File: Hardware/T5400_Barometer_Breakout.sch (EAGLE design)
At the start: 13 parts, among them U1 T5400

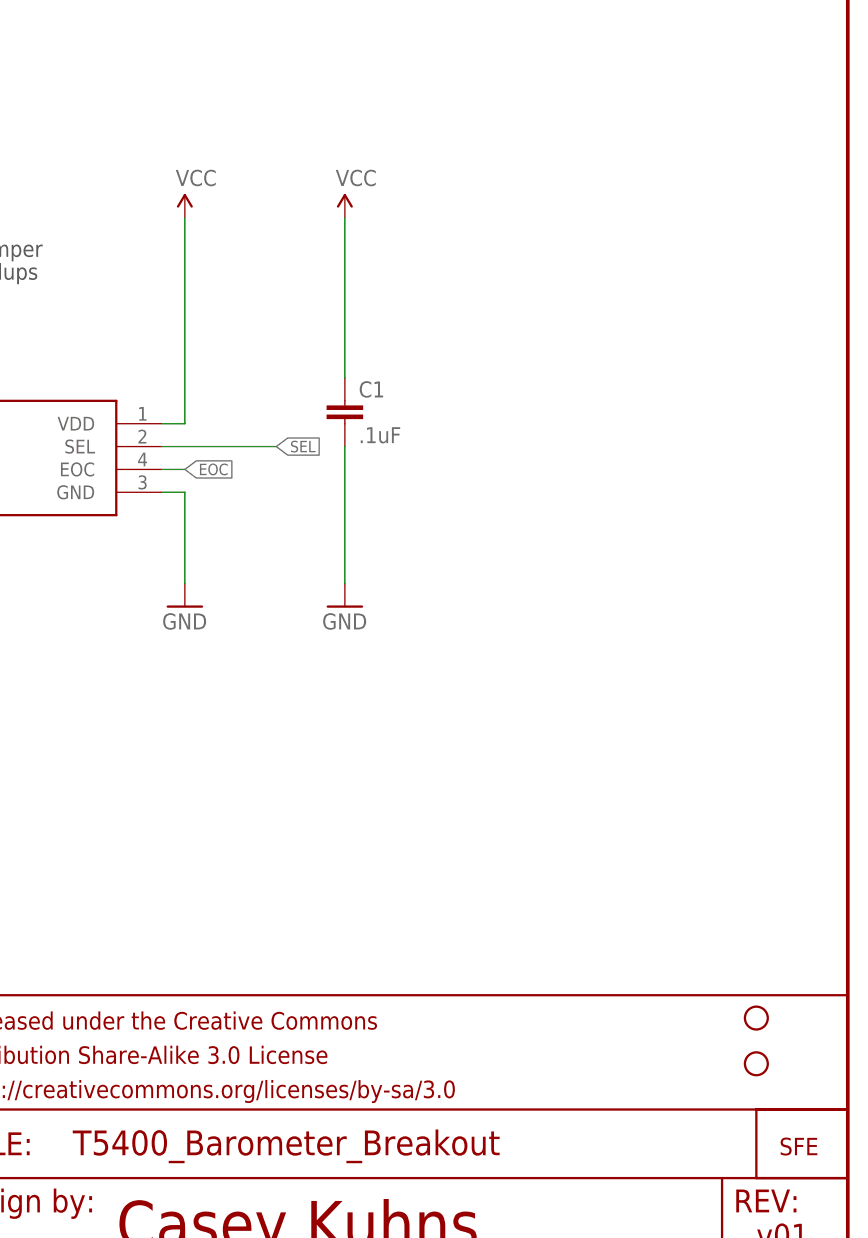
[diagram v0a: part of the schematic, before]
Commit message: updated with mode pullup and larger board
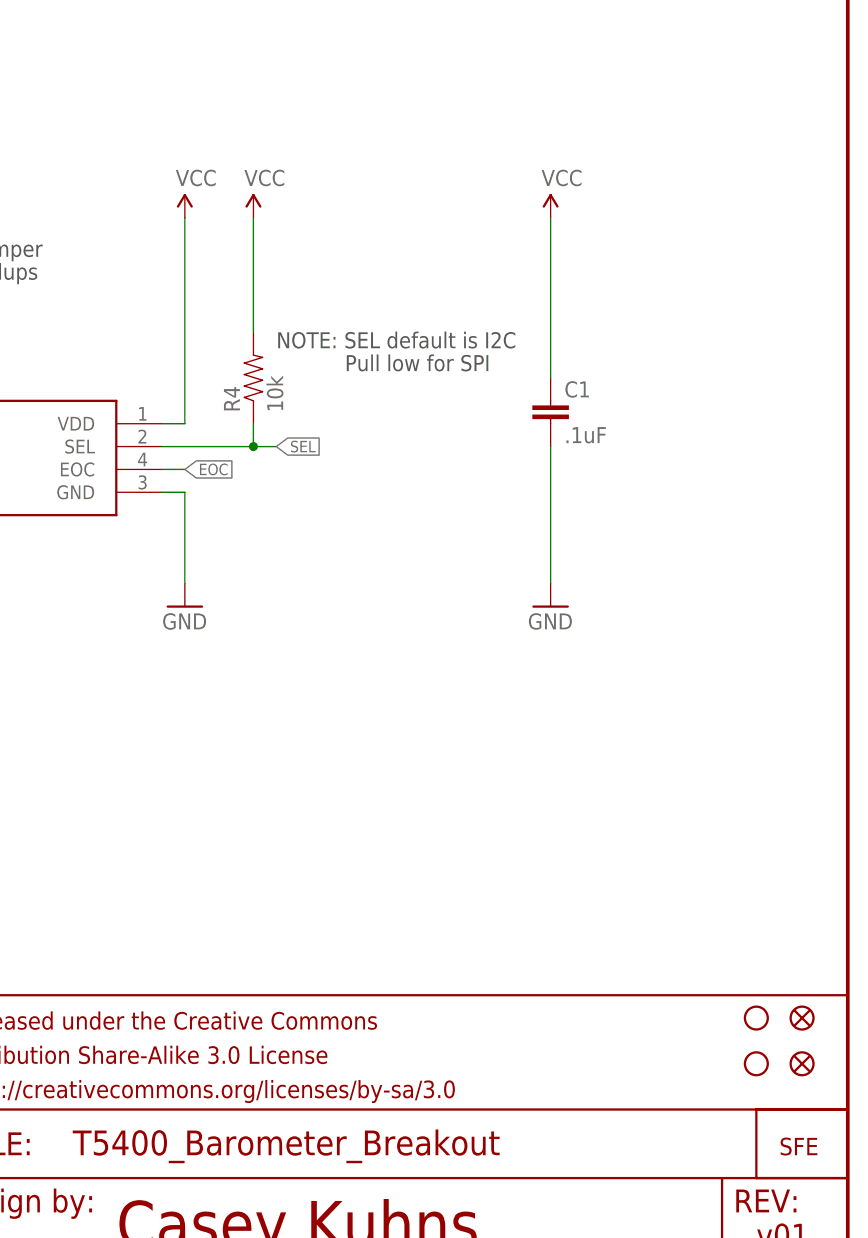
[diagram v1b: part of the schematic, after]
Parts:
- added FID1, FID2: FIDUCIAL1X2, SparkFun-Aesthetics:FIDUCIAL1X2
- added R4: 10k, SparkFun-Passives:RESISTOR0603-RES
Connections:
- net SEL: now also R4.1
- net VCC: now also R4.2
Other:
- note added: "NOTE: SEL default is I2C"
- note added: "Pull low for SPI"
- moved on the sheet: C1
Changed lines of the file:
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@@
 <?xml version="1.0" encoding="utf-8"?>
 <!DOCTYPE eagle SYSTEM "eagle.dtd">
-<eagle version="6.5.0">
+<eagle version="6.0">
 <drawing>
 <settings>
@@
 <part name="R3" library="SparkFun-Passives" deviceset="RESISTOR" device="0603-RES" value="10k"/>
 <part name="SUPPLY6" library="SparkFun-Aesthetics" deviceset="VCC" device=""/>
+<part name="FID1" library="SparkFun-Aesthetics" deviceset="FIDUCIAL" device="1X2"/>
+<part name="FID2" library="SparkFun-Aesthetics" deviceset="FIDUCIAL" device="1X2"/>
 <part name="LOGO3" library="SparkFun-Aesthetics" deviceset="SFE_LOGO_FLAME" device=".1_INCH"/>
 <part name="SJ2" library="SparkFun-Passives" deviceset="SOLDERJUMPER_2WAY" device="PASTE1&amp;2&amp;3"/>
 <part name="SUPPLY2" library="SparkFun-Aesthetics" deviceset="VCC" device=""/>
+<part name="R4" library="SparkFun-Passives" deviceset="RESISTOR" device="0603-RES" value="10k"/>
+<part name="SUPPLY3" library="SparkFun-Aesthetics" deviceset="VCC" device=""/>
 </parts>
 <sheets>
@@
 <text x="134.62" y="116.84" size="1.778" layer="97" rot="MR180"> to disable I2C pullups</text>
 <rectangle x1="122.682" y1="113.792" x2="126.492" y2="114.808" layer="94"/>
+<text x="185.42" y="109.22" size="1.778" layer="97" rot="R180" align="bottom-right">NOTE: SEL default is I2C</text>
+<text x="193.04" y="106.68" size="1.778" layer="97" rot="MR180">Pull low for SPI</text>
 </plain>
 <instances>
@@
 <instance part="R2" gate="G$1" x="116.84" y="106.68" rot="R90"/>
 <instance part="SUPPLY1" gate="1" x="175.26" y="121.92"/>
-<instance part="C1" gate="G$1" x="193.04" y="99.06"/>
-<instance part="SUPPLY5" gate="1" x="193.04" y="121.92"/>
-<instance part="GND3" gate="1" x="193.04" y="78.74"/>
+<instance part="C1" gate="G$1" x="215.9" y="99.06"/>
+<instance part="SUPPLY5" gate="1" x="215.9" y="121.92"/>
+<instance part="GND3" gate="1" x="215.9" y="78.74"/>
 <instance part="SUPPLY4" gate="1" x="68.58" y="121.92"/>
 <instance part="GND2" gate="1" x="81.28" y="78.74"/>
@@
 <instance part="R3" gate="G$1" x="99.06" y="99.06" rot="R90"/>
 <instance part="SUPPLY6" gate="1" x="99.06" y="121.92"/>
+<instance part="FID1" gate="G$1" x="243.84" y="27.94"/>
+<instance part="FID2" gate="G$1" x="243.84" y="33.02"/>
 <instance part="LOGO3" gate="G$1" x="132.08" y="20.32"/>
 <instance part="SJ2" gate="G$1" x="124.46" y="114.3" rot="R270"/>
 <instance part="SUPPLY2" gate="1" x="124.46" y="121.92"/>
+<instance part="R4" gate="G$1" x="182.88" y="104.14" rot="R90"/>
+<instance part="SUPPLY3" gate="1" x="182.88" y="121.92"/>
 </instances>
 <busses>
@@
 <pinref part="C1" gate="G$1" pin="2"/>
 <pinref part="GND3" gate="1" pin="GND"/>
-<wire x1="193.04" y1="81.28" x2="193.04" y2="96.52" width="0.1524" layer="91"/>
+<wire x1="215.9" y1="81.28" x2="215.9" y2="96.52" width="0.1524" layer="91"/>
 </segment>
 <segment>
@@
 <segment>
 <pinref part="U1" gate="U$1" pin="SEL"/>
-<wire x1="172.72" y1="96.52" x2="185.42" y2="96.52" width="0.1524" layer="91"/>
+<wire x1="172.72" y1="96.52" x2="182.88" y2="96.52" width="0.1524" layer="91"/>
 <label x="185.42" y="96.52" size="1.27" layer="95" xref="yes"/>
+<pinref part="R4" gate="G$1" pin="1"/>
+<wire x1="182.88" y1="96.52" x2="185.42" y2="96.52" width="0.1524" layer="91"/>
+<wire x1="182.88" y1="99.06" x2="182.88" y2="96.52" width="0.1524" layer="91"/>
+<junction x="182.88" y="96.52"/>
 </segment>
 <segment>
@@
 <pinref part="C1" gate="G$1" pin="1"/>
 <pinref part="SUPPLY5" gate="1" pin="VCC"/>
-<wire x1="193.04" y1="121.92" x2="193.04" y2="104.14" width="0.1524" layer="91"/>
+<wire x1="215.9" y1="121.92" x2="215.9" y2="104.14" width="0.1524" layer="91"/>
 </segment>
 <segment>
@@
 <wire x1="124.46" y1="121.92" x2="124.46" y2="119.38" width="0.1524" layer="91"/>
 </segment>
-</net>
+<segment>
+<pinref part="R4" gate="G$1" pin="2"/>
+<pinref part="SUPPLY3" gate="1" pin="VCC"/>
+<wire x1="182.88" y1="121.92" x2="182.88" y2="109.22" width="0.1524" layer="91"/>
+</segment>
+</net>

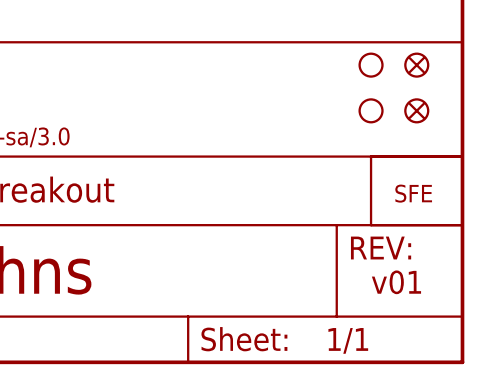
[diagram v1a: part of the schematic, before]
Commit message: changed version and modified pads for production
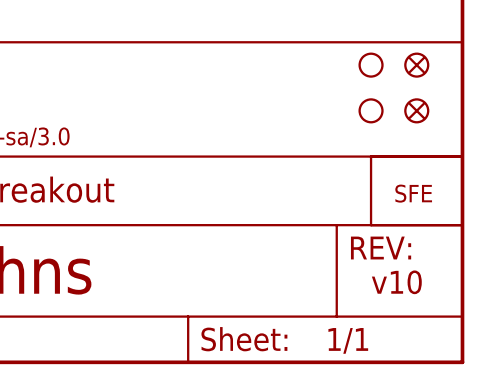
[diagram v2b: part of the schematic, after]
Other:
- note added: "v10"
- note removed: "v01"
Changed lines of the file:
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@@
 <plain>
 <text x="167.64" y="7.62" size="5.08" layer="94" font="vector">Casey Kuhns</text>
-<text x="238.76" y="7.62" size="2.54" layer="94" font="vector">v01</text>
+<text x="238.76" y="7.62" size="2.54" layer="94" font="vector">v10</text>
 <text x="127" y="119.38" size="1.778" layer="97" rot="R180" align="bottom-right">NOTE: Remove solder jumper</text>
 <text x="134.62" y="116.84" size="1.778" layer="97" rot="MR180"> to disable I2C pullups</text>
